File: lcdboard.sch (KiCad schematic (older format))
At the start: 71 parts, among them J1 Conn_02x05_Odd_Even, J2 Conn_02x25_Counter_Clockwise, J3 Conn_02x12_Counter_Clockwise, J4 USB_B_Micro, J5 Conn_01x03, SW1 SW_Push, SW3 SW_SPST, U1 MK82FN256VLL15, U2 Serial-Flash, U3 TPS61169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

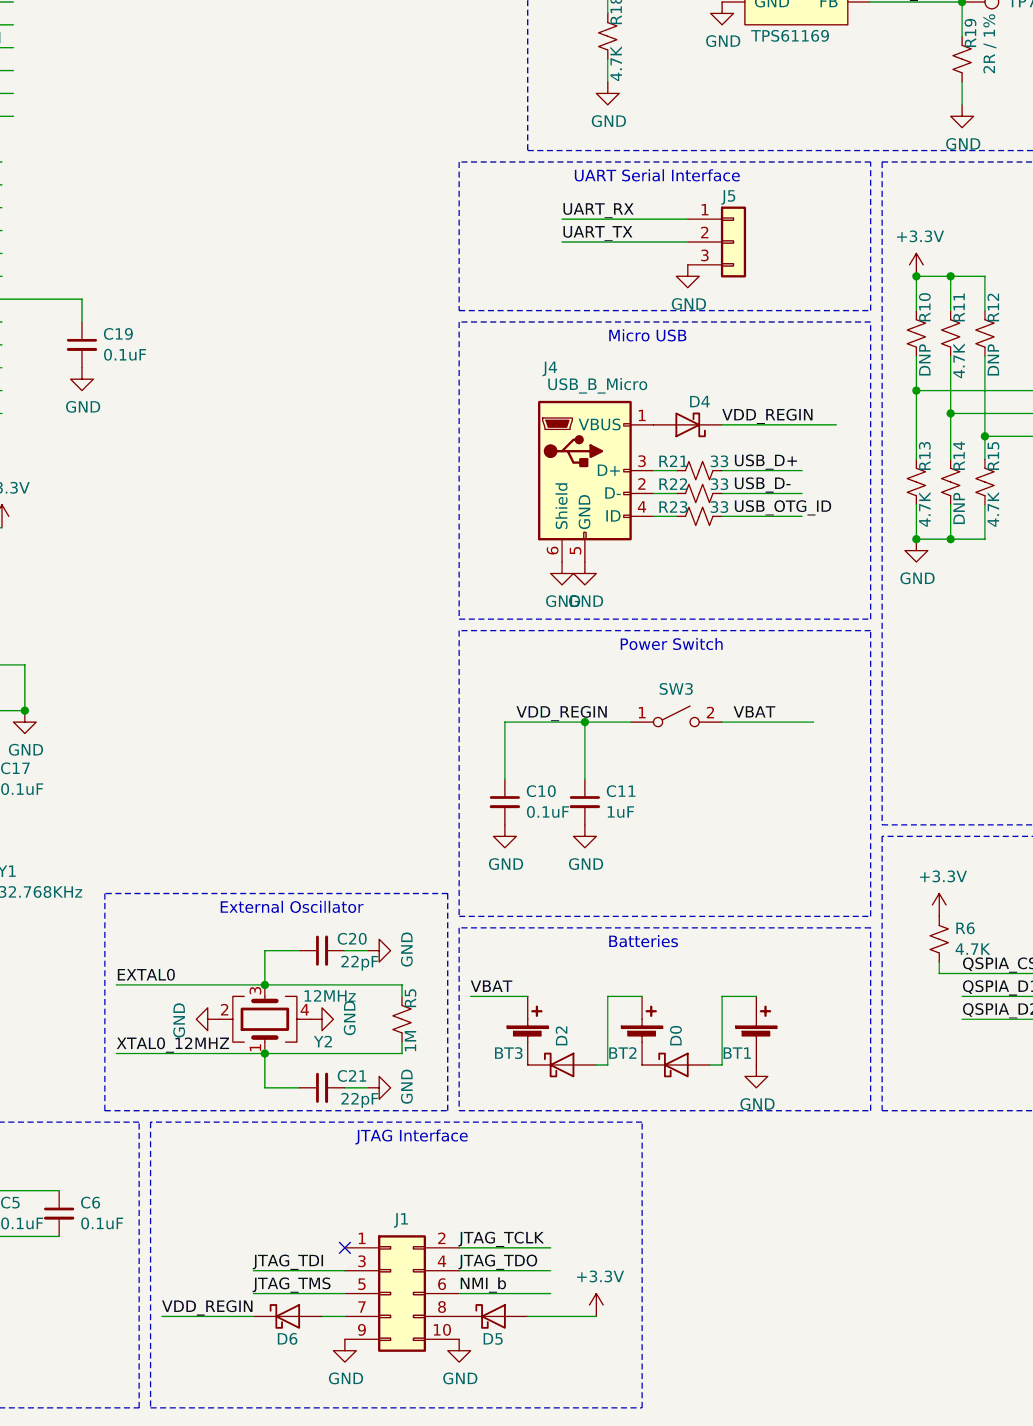
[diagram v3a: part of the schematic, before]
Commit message: Rewire JTAG & UART to use 6-pin connectors
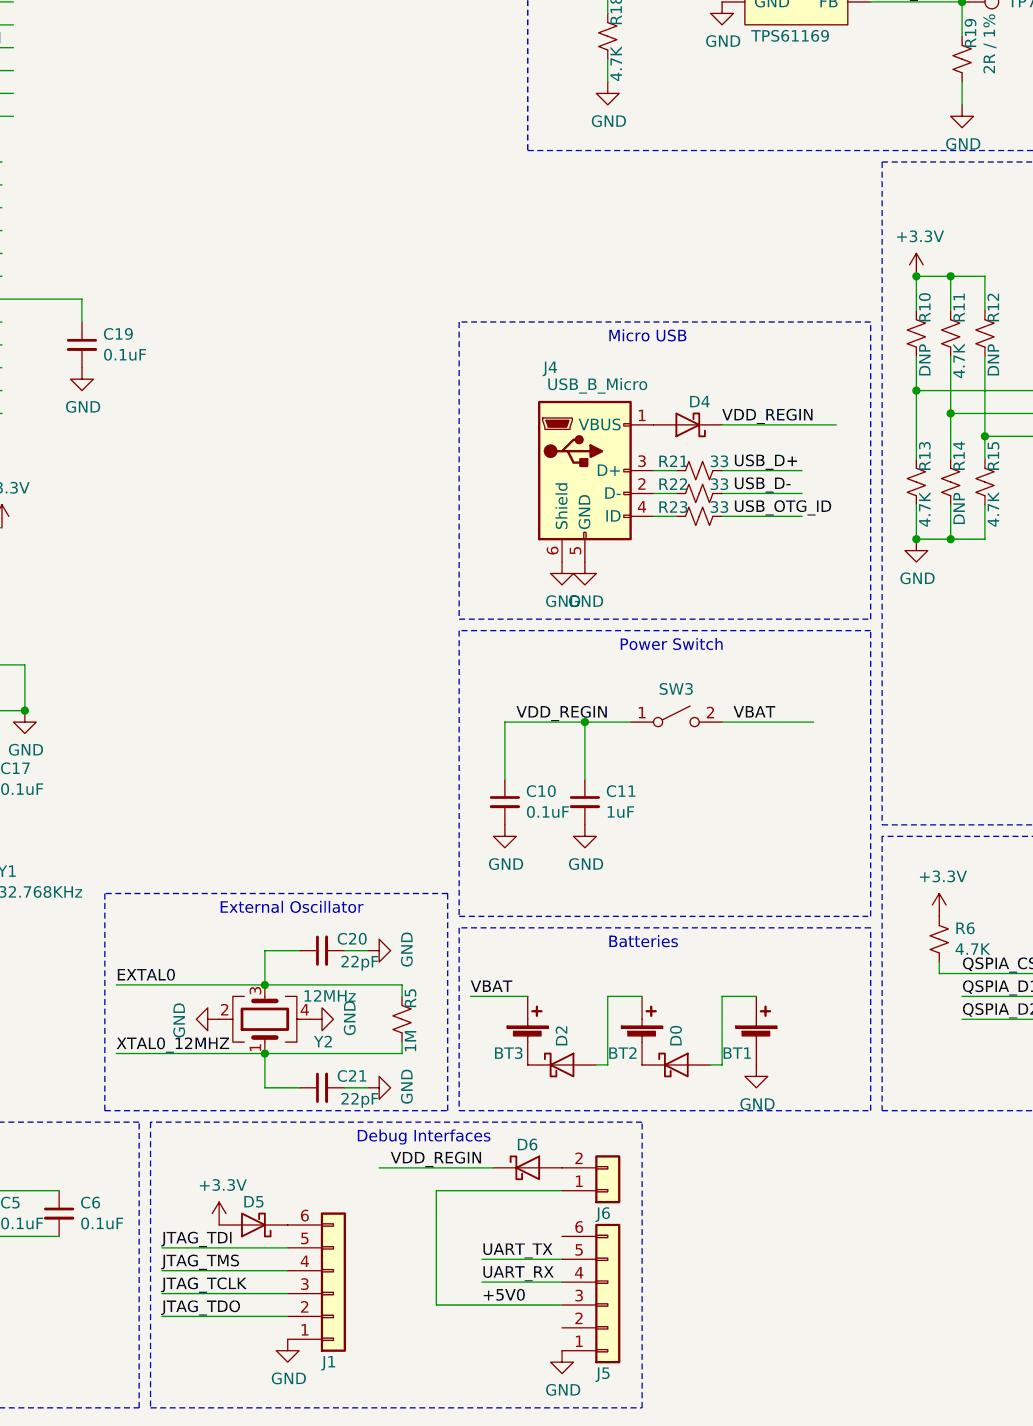
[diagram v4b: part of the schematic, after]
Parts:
- removed J1: Conn_02x05_Odd_Even, Connector_PinHeader_2.54mm:PinHeader_2x05_P2.54mm_Vertical, symbol Connector_Generic:Conn_02x05_Odd_Even
- removed J5: Conn_01x03, Connector_PinHeader_2.54mm:PinHeader_1x03_P2.54mm_Vertical, symbol Connector_Generic:Conn_01x03
- added J1, J5: Conn_01x06, Connector_PinHeader_2.54mm:PinHeader_1x06_P2.54mm_Horizontal, symbol Connector_Generic:Conn_01x06
- added J6: Conn_01x02, Connector_PinHeader_2.54mm:PinHeader_1x02_P2.54mm_Horizontal, symbol Connector_Generic:Conn_01x02
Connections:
- net labels added: +5V0
- no-connect marks 14 -> 13
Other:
- note added: "Debug Interfaces"
- note removed: "JTAG Interface"
- note removed: "UART Serial Interface"
- moved on the sheet: D5
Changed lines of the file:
@@
 Wire Wire Line
 	2600 6250 2700 6250
-Text Notes 5650 6600 0    50   ~ 0
-JTAG Interface
-Wire Wire Line
-	5200 7150 5600 7150
-Wire Wire Line
-	5200 7250 5600 7250
-Wire Wire Line
-	4800 7350 5200 7350
-Wire Wire Line
-	6100 7050 6500 7050
-Wire Wire Line
-	6100 7150 6500 7150
-Text Label 4800 7350 0    50   ~ 0
-VDD_REGIN
-$Comp
-L power:GND #PWR0114
-U 1 1 5C69D70B
-P 6100 7450
-F 0 "#PWR0114" H 6100 7200 50  0001 C CNN
-F 1 "GND" H 6105 7277 50  0000 C CNN
-F 2 "" H 6100 7450 50  0001 C CNN
-F 3 "" H 6100 7450 50  0001 C CNN
-	1    6100 7450
-	1    0    0    -1
-$EndComp
-Text Label 6100 7050 0    50   ~ 0
-JTAG_TCLK
-Text Label 5200 7150 0    50   ~ 0
-JTAG_TDI
-Text Label 6100 7150 0    50   ~ 0
-JTAG_TDO
-Text Label 5200 7250 0    50   ~ 0
-JTAG_TMS
 Wire Notes Line
 	4750 6500 4750 7750
@@
 Text Label 900  1700 0    50   ~ 0
 JTAG_TMS
-$Comp
-L power:GND #PWR0115
-U 1 1 5C6BDBFE
-P 5600 7450
-F 0 "#PWR0115" H 5600 7200 50  0001 C CNN
-F 1 "GND" H 5605 7277 50  0000 C CNN
-F 2 "" H 5600 7450 50  0001 C CNN
-F 3 "" H 5600 7450 50  0001 C CNN
-	1    5600 7450
-	1    0    0    -1
-$EndComp
-Text Label 6100 7250 0    50   ~ 0
-NMI_b
-Wire Wire Line
-	6100 7250 6500 7250
-$Comp
-L Connector_Generic:Conn_02x05_Odd_Even J1
-U 1 1 5C6C066E
-P 5800 7250
-F 0 "J1" H 5850 7575 50  0000 C CNN
-F 1 "Conn_02x05_Odd_Even" H 5850 7576 50  0001 C CNN
-F 2 "Connector_PinHeader_2.54mm:PinHeader_2x05_P2.54mm_Vertical" H 5800 7250 50  0001 C CNN
-F 3 "~" H 5800 7250 50  0001 C CNN
-F 4 "" H 0   0   50  0001 C CNN "MFR"
-F 5 "" H 0   0   50  0001 C CNN "MPN"
-	1    5800 7250
-	1    0    0    -1
-$EndComp
 Connection ~ 1650 7050
 $Comp
@@
 Wire Wire Line
 	750  3600 1300 3600
-Text Label 6550 2550 0    50   ~ 0
-UART_RX
-Text Label 6550 2650 0    50   ~ 0
-UART_TX
-Wire Wire Line
-	6550 2550 7100 2550
-Wire Wire Line
-	6550 2650 7100 2650
-$Comp
-L power:GND #PWR0151
-U 1 1 5CBA90B3
-P 7100 2750
-F 0 "#PWR0151" H 7100 2500 50  0001 C CNN
-F 1 "GND" H 7105 2577 50  0000 C CNN
-F 2 "" H 7100 2750 50  0001 C CNN
-F 3 "" H 7100 2750 50  0001 C CNN
-	1    7100 2750
-	1    0    0    -1
-$EndComp
-$Comp
-L Connector_Generic:Conn_01x03 J5
-U 1 1 5CC2515C
-P 7300 2650
-F 0 "J5" H 7250 2850 50  0000 L CNN
-F 1 "Conn_01x03" H 7380 2601 50  0001 L CNN
-F 2 "Connector_PinHeader_2.54mm:PinHeader_1x03_P2.54mm_Vertical" H 7300 2650 50  0001 C CNN
-F 3 "~" H 7300 2650 50  0001 C CNN
-	1    7300 2650
-	1    0    0    -1
-$EndComp
-Wire Notes Line
-	6100 2950 7900 2950
-Wire Notes Line
-	7900 2950 7900 2300
-Wire Notes Line
-	7900 2300 6100 2300
-Wire Notes Line
-	6100 2300 6100 2950
-Text Notes 6600 2400 0    50   ~ 0
-UART Serial Interface
 $Comp
 L Device:R_Small_US R24
@@
 Wire Wire Line
 	10600 3300 10600 3000
-$Comp
-L power:+3.3V #PWR0153
-U 1 1 5CD698F8
-P 6700 7350
-F 0 "#PWR0153" H 6700 7200 50  0001 C CNN
-F 1 "+3.3V" H 6715 7523 50  0000 C CNN
-F 2 "" H 6700 7350 50  0001 C CNN
-F 3 "" H 6700 7350 50  0001 C CNN
-	1    6700 7350
-	1    0    0    -1
-$EndComp
-Wire Wire Line
-	5500 7350 5600 7350
-$Comp
-L Device:D_Schottky D6
-U 1 1 5CEC95EC
-P 5350 7350
-F 0 "D6" H 5300 7250 50  0000 L CNN
-F 1 "D_Schottky" V 5395 7429 50  0001 L CNN
-F 2 "Diode_SMD:D_SOT-23_ANK" H 5350 7350 50  0001 C CNN
-F 3 "~" H 5350 7350 50  0001 C CNN
-F 4 "ROHM" H 0   0   50  0001 C CNN "MFR"
-F 5 "BAT54SHMFHT116" H 0   0   50  0001 C CNN "MPN"
-	1    5350 7350
-	1    0    0    -1
-$EndComp
-$Comp
-L Device:D_Schottky D5
-U 1 1 5CF92390
-P 6250 7350
-F 0 "D5" H 6200 7250 50  0000 L CNN
-F 1 "D_Schottky" V 6295 7429 50  0001 L CNN
-F 2 "Diode_SMD:D_SOT-23_ANK" H 6250 7350 50  0001 C CNN
-F 3 "~" H 6250 7350 50  0001 C CNN
-F 4 "ROHM" H 0   0   50  0001 C CNN "MFR"
-F 5 "BAT54SHMFHT116" H 0   0   50  0001 C CNN "MPN"
-	1    6250 7350
-	1    0    0    -1
-$EndComp
-Wire Wire Line
-	6400 7350 6700 7350
 $Comp
 L Connector:TestPoint TP3
@@
 Wire Wire Line
 	650  1800 1300 1800
-NoConn ~ 5600 7050
+Text Notes 5650 6600 0    50   ~ 0
+Debug Interfaces
+Wire Wire Line
+	4800 7050 5350 7050
+Wire Wire Line
+	4800 7150 5350 7150
+Wire Wire Line
+	4800 7250 5350 7250
+Wire Wire Line
+	4800 7350 5350 7350
+$Comp
+L power:GND #PWR0114
+U 1 1 5C69D70B
+P 5350 7450
+F 0 "#PWR0114" H 5350 7200 50  0001 C CNN
+F 1 "GND" H 5355 7277 50  0000 C CNN
+F 2 "" H 5350 7450 50  0001 C CNN
+F 3 "" H 5350 7450 50  0001 C CNN
+	1    5350 7450
+	1    0    0    -1
+$EndComp
+Text Label 4800 7250 0    50   ~ 0
+JTAG_TCLK
+Text Label 4800 7050 0    50   ~ 0
+JTAG_TDI
+Text Label 4800 7350 0    50   ~ 0
+JTAG_TDO
+Text Label 4800 7150 0    50   ~ 0
+JTAG_TMS
+$Comp
+L power:+3.3V #PWR0153
+U 1 1 5CD698F8
+P 5050 6950
+F 0 "#PWR0153" H 5050 6800 50  0001 C CNN
+F 1 "+3.3V" H 5065 7123 50  0000 C CNN
+F 2 "" H 5050 6950 50  0001 C CNN
+F 3 "" H 5050 6950 50  0001 C CNN
+	1    5050 6950
+	1    0    0    -1
+$EndComp
+$Comp
+L Device:D_Schottky D5
+U 1 1 5CF92390
+P 5200 6950
+F 0 "D5" H 5150 6850 50  0000 L CNN
+F 1 "D_Schottky" V 5245 7029 50  0001 L CNN
+F 2 "Diode_SMD:D_SOT-23_ANK" H 5200 6950 50  0001 C CNN
+F 3 "~" H 5200 6950 50  0001 C CNN
+F 4 "ROHM" H -1050 -400 50  0001 C CNN "MFR"
+F 5 "BAT54SHMFHT116" H -1050 -400 50  0001 C CNN "MPN"
+	1    5200 6950
+	-1   0    0    1
+$EndComp
+$Comp
+L Connector_Generic:Conn_01x06 J1
+U 1 1 5DA3F00B
+P 5550 7250
+F 0 "J1" H 5500 7550 50  0000 L CNN
+F 1 "Conn_01x06" H 5630 7151 50  0001 L CNN
+F 2 "Connector_PinHeader_2.54mm:PinHeader_1x06_P2.54mm_Horizontal" H 5550 7250 50  0001 C CNN
+F 3 "~" H 5550 7250 50  0001 C CNN
+	1    5550 7250
+	1    0    0    1
+$EndComp
+$Comp
+L Connector_Generic:Conn_01x06 J5
+U 1 1 5E08D484
+P 6750 7300
+F 0 "J5" H 6700 7600 50  0000 L CNN
+F 1 "Conn_01x06" H 6830 7201 50  0001 L CNN
+F 2 "Connector_PinHeader_2.54mm:PinHeader_1x06_P2.54mm_Horizontal" H 6750 7300 50  0001 C CNN
+F 3 "~" H 6750 7300 50  0001 C CNN
+	1    6750 7300
+	1    0    0    1
+$EndComp
+$Comp
+L power:GND #PWR04
+U 1 1 5E0B297C
+P 6550 7500
+F 0 "#PWR04" H 6550 7250 50  0001 C CNN
+F 1 "GND" H 6555 7327 50  0000 C CNN
+F 2 "" H 6550 7500 50  0001 C CNN
+F 3 "" H 6550 7500 50  0001 C CNN
+	1    6550 7500
+	1    0    0    -1
+$EndComp
+Text Label 6200 7200 0    50   ~ 0
+UART_RX
+Text Label 6200 7100 0    50   ~ 0
+UART_TX
+Wire Wire Line
+	6200 7200 6550 7200
+Wire Wire Line
+	6200 7100 6550 7100
+Text Label 6200 7300 0    50   ~ 0
++5V0
+$Comp
+L Device:D_Schottky D6
+U 1 1 5E1CD1EC
+P 6400 6700
+F 0 "D6" H 6350 6800 50  0000 L CNN
+F 1 "D_Schottky" V 6445 6779 50  0001 L CNN
+F 2 "Diode_SMD:D_SOT-23_ANK" H 6400 6700 50  0001 C CNN
+F 3 "~" H 6400 6700 50  0001 C CNN
+F 4 "ROHM" H 150 -650 50  0001 C CNN "MFR"
+F 5 "BAT54SHMFHT116" H 150 -650 50  0001 C CNN "MPN"
+	1    6400 6700
+	1    0    0    -1
+$EndComp
+$Comp
+L Connector_Generic:Conn_01x02 J6
+U 1 1 5E237CB0
+P 6750 6800
+F 0 "J6" H 6700 6900 50  0000 L CNN
+F 1 "Conn_01x02" H 6830 6701 50  0001 L CNN
+F 2 "Connector_PinHeader_2.54mm:PinHeader_1x02_P2.54mm_Horizontal" H 6750 6800 50  0001 C CNN
+F 3 "~" H 6750 6800 50  0001 C CNN
+	1    6750 6800
+	1    0    0    1
+$EndComp
+Wire Wire Line
+	5750 6700 6250 6700
+Text Label 5800 6700 0    50   ~ 0
+VDD_REGIN
+Wire Wire Line
+	6000 6800 6550 6800
+Wire Wire Line
+	6000 7300 6550 7300
+Wire Wire Line
+	6000 6800 6000 7300
 $EndSCHEMATC

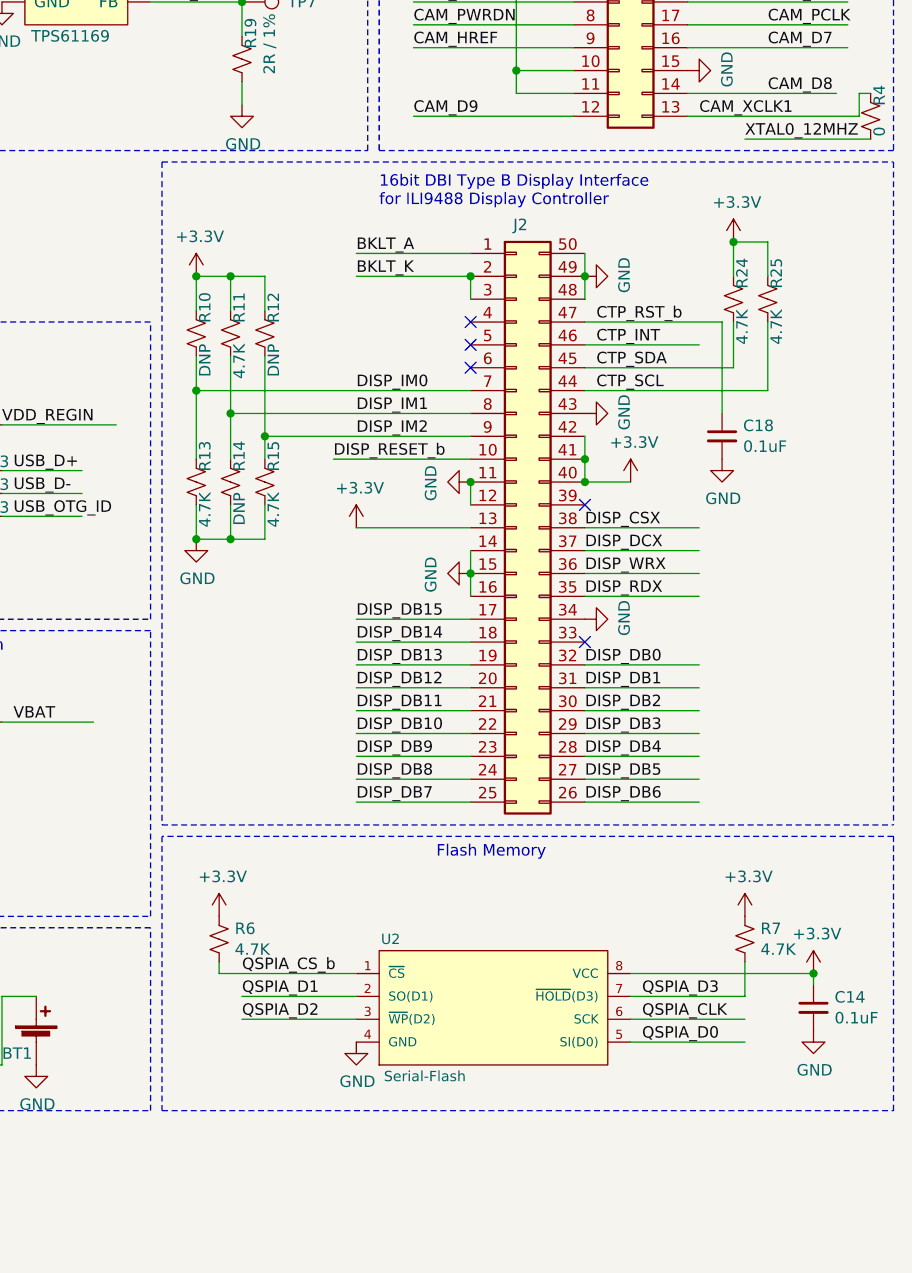
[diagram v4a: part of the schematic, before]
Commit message: Add r-packs to LCD signals to reduce EMI
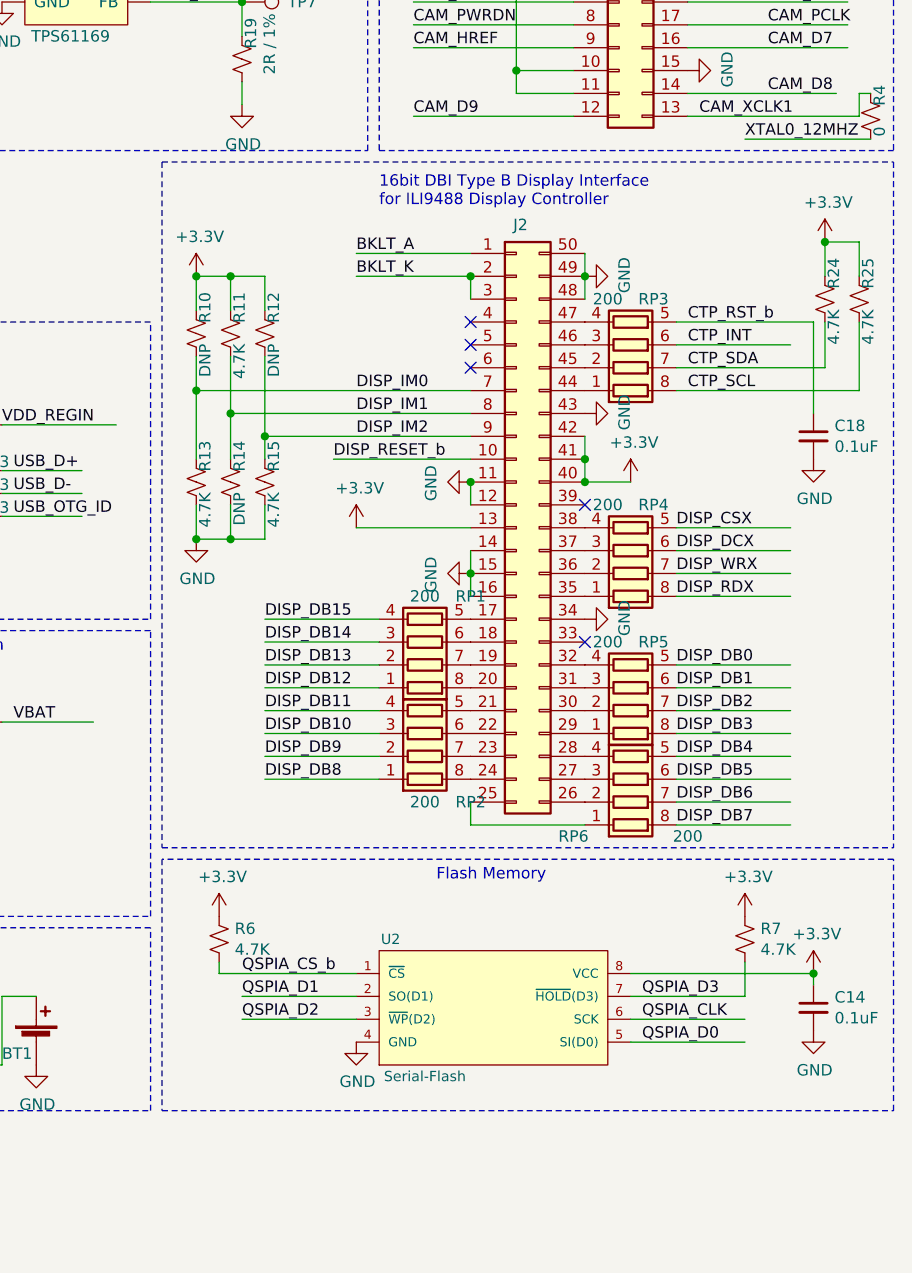
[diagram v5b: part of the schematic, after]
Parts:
- added RP1, RP2, RP3, RP4, RP5, RP6: 200, Resistor_SMD:R_Array_Concave_4x0402, symbol Device:R_Pack04
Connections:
- wire segments 280 -> 282
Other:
- moved on the sheet: C18, R24, R25
